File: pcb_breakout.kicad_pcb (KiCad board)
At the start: 2 copper layers, 87 x 30 mm, 3 parts, among them P1 CONN_01X32, P2 CONN_02X03, U1 ET024002DMU

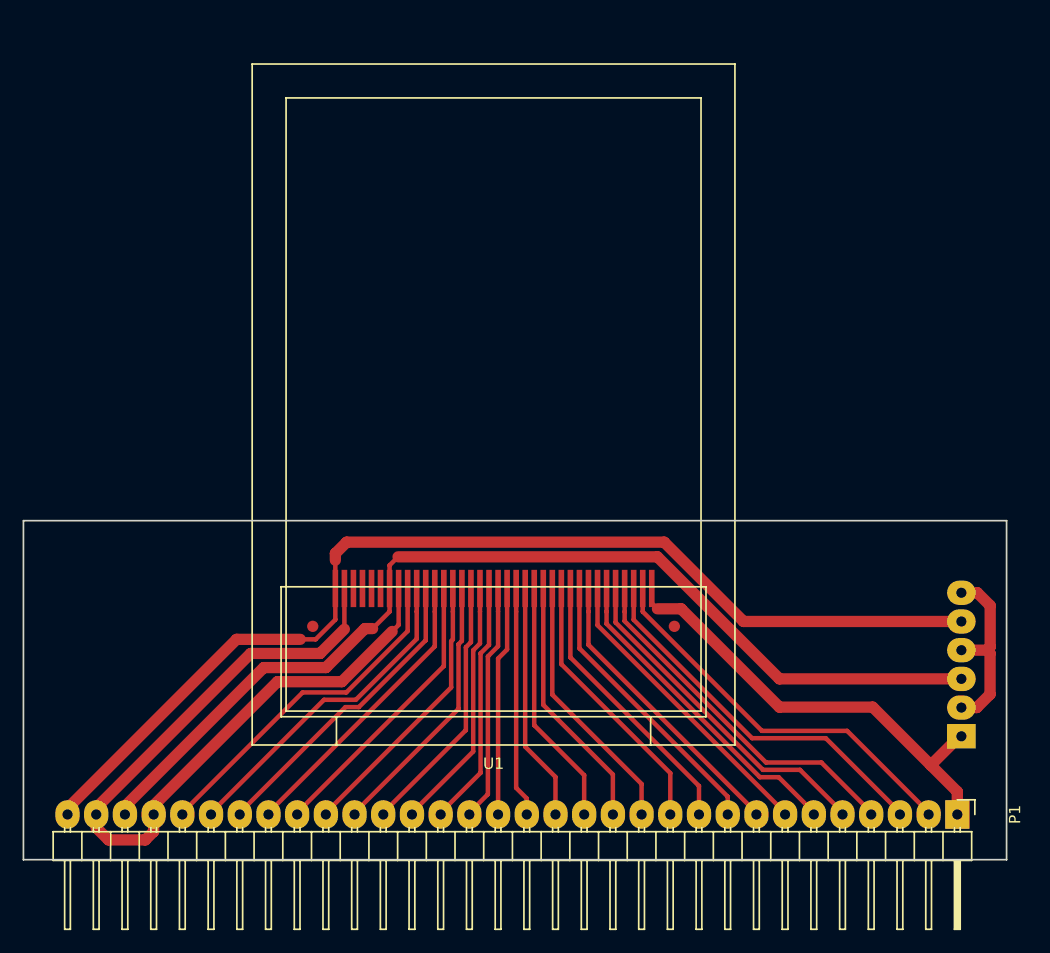
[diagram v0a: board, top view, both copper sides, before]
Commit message: Extend pcb outline + identifying text
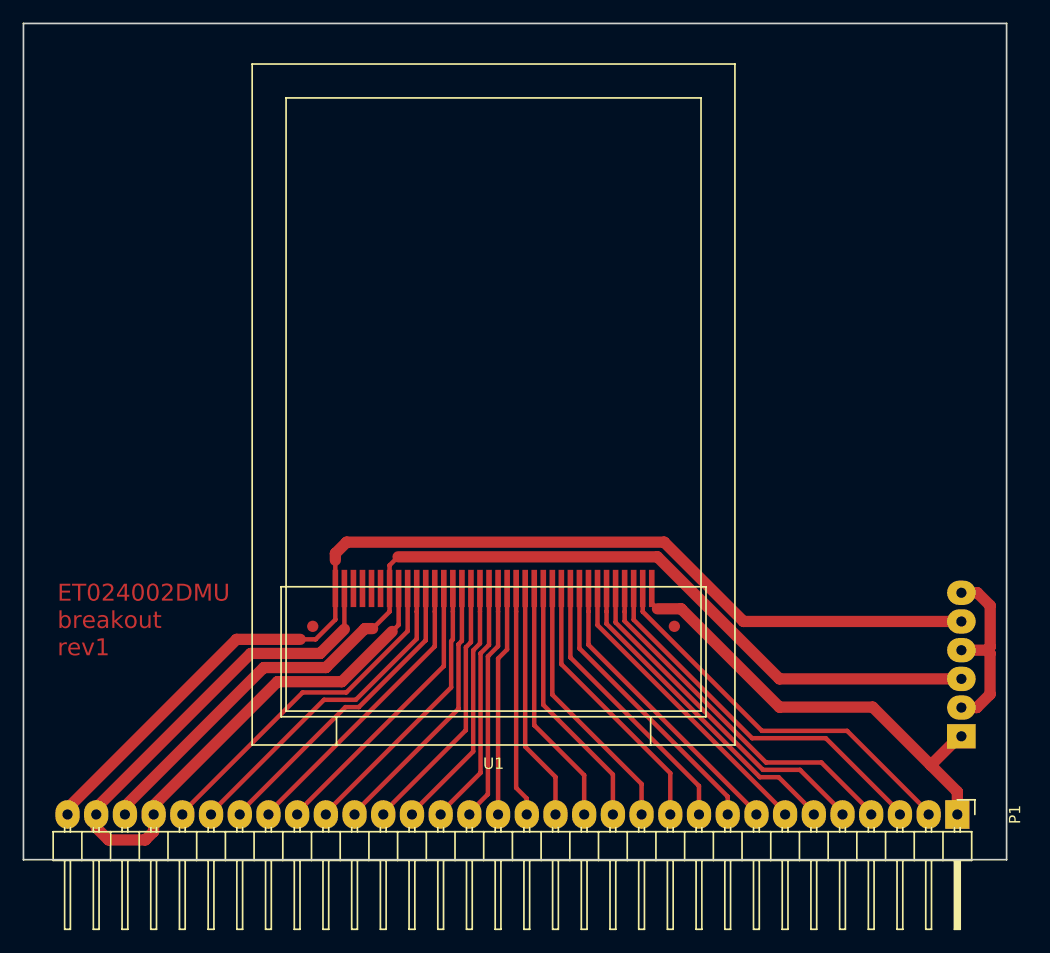
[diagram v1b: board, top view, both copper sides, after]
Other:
- board size 87 x 30 mm -> 87 x 74 mm
- board text added: "ET024002DMU breakout rev1"
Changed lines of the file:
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@@
     (area 57.924999 51.5125 151.925001 130.925001)
     (thickness 1.6)
-    (drawings 4)
+    (drawings 5)
     (tracks 178)
     (zones 0)
@@
   )
   (setup
-    (last_trace_width 1)
+    (last_trace_width 0.4)
     (user_trace_width 1)
     (trace_clearance 0.25)
@@
     (pad "" smd circle (at 16 3.35) (size 1 1) (layers F.Cu F.Paste F.Mask))
   )
-  (gr_line (start 58 94) (end 58 124) (layer Edge.Cuts) (width 0.15))
-  (gr_line (start 145 94) (end 58 94) (layer Edge.Cuts) (width 0.15))
-  (gr_line (start 145 124) (end 145 94) (layer Edge.Cuts) (width 0.15))
+  (gr_text "ET024002DMU\nbreakout\nrev1" (at 61 102.8) (layer F.Cu)
+    (effects (font (size 1.5 1.5) (thickness 0.3)) (justify left))
+  )
+  (gr_line (start 58 50) (end 58 124) (layer Edge.Cuts) (width 0.15))
+  (gr_line (start 145 50) (end 58 50) (layer Edge.Cuts) (width 0.15))
+  (gr_line (start 145 124) (end 145 50) (layer Edge.Cuts) (width 0.15))
   (gr_line (start 58 124) (end 145 124) (layer Edge.Cuts) (width 0.15))
   (segment (start 138.3 115.644) (end 140.64 117.984) (width 1) (layer F.Cu) (net 1))

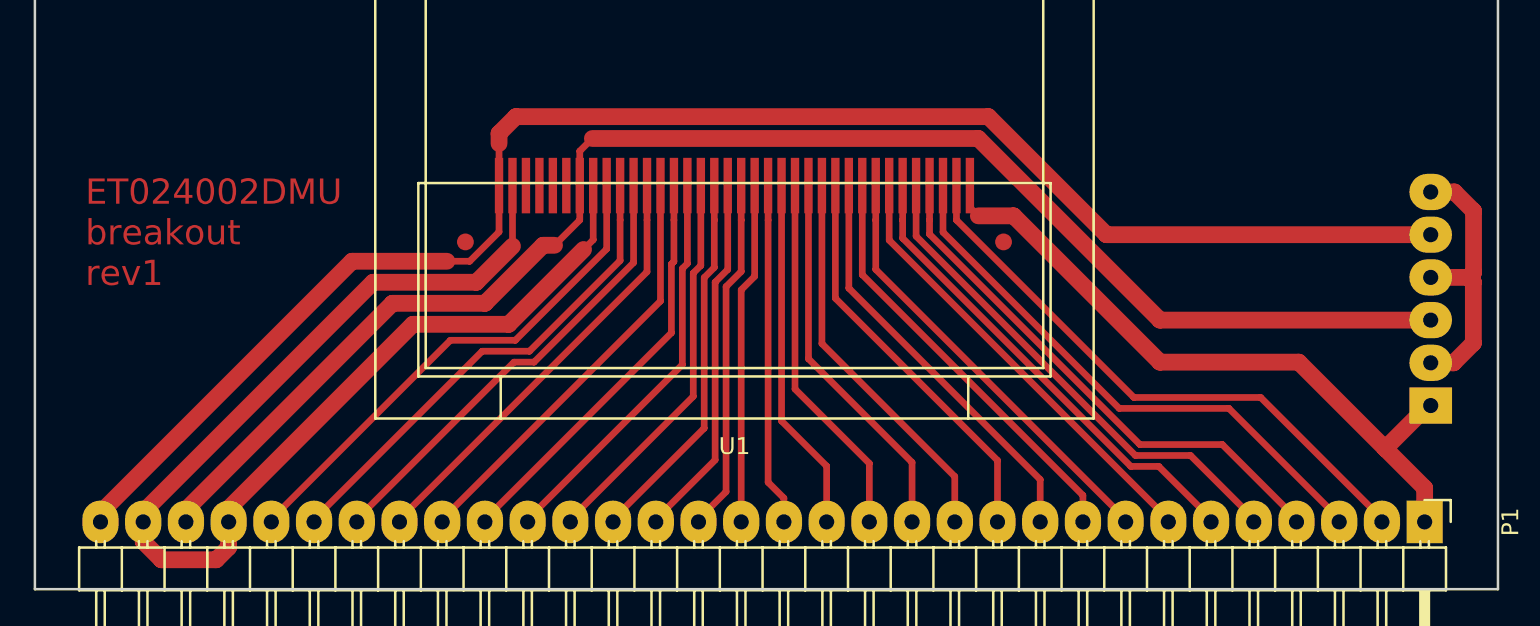
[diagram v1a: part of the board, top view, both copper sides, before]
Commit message: Move tracks a bit to create larger clearance
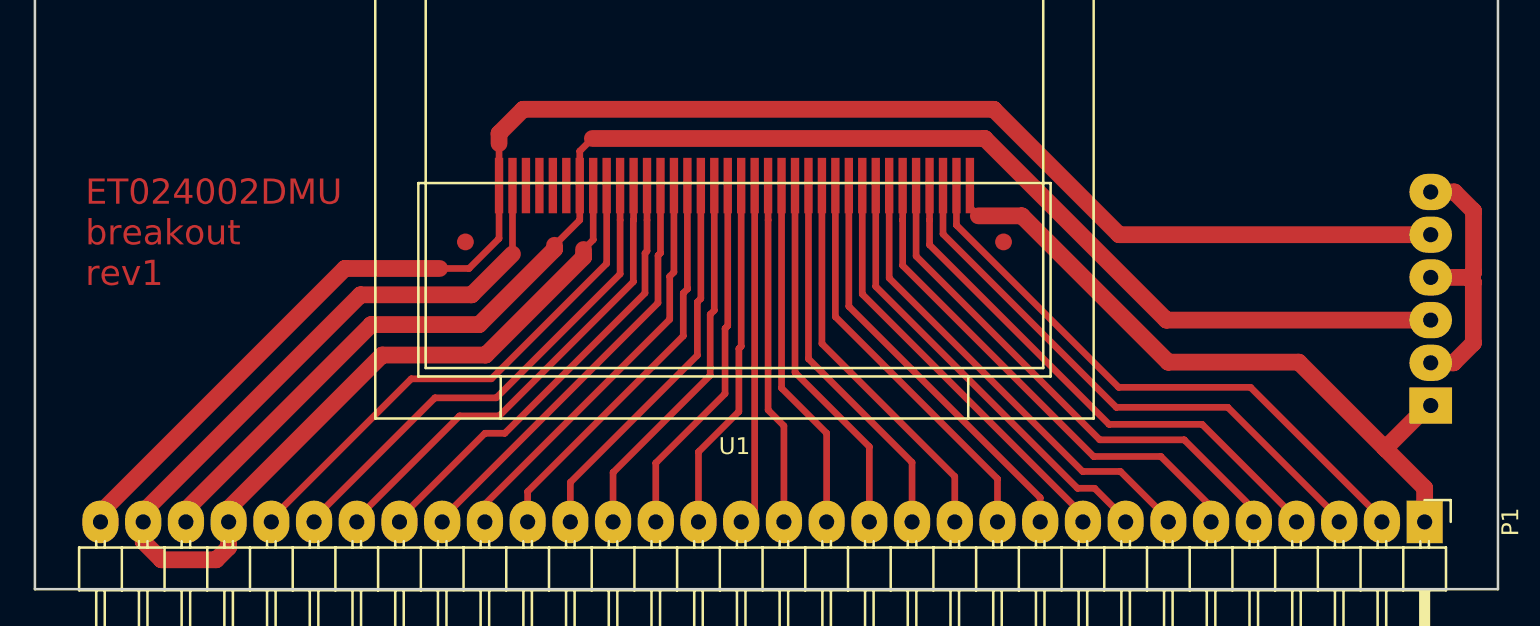
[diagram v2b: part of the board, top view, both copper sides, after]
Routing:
- net /te: track 28.6 -> 29.9 mm
- net /db17: track 26.9 -> 28.2 mm
- net /im2: track 30.2 -> 31.3 mm
- net /rd: track 26.1 -> 26.8 mm
- net /wr: track 27.5 -> 28.2 mm
- net /db16: track 26.2 -> 26.7 mm
- net /led+: track 95.7 -> 96.3 mm
- net GND: track 73.5 -> 74.1 mm
- net /cs: track 30.5 -> 31.1 mm
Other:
- net class Default: clearance 0.25 -> 0.295
- rule trace_clearance: 0.25 -> 0.295
